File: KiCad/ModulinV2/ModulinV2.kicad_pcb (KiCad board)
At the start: 2 copper layers, 654 parts, among them IC1 TL074HIDR, IC10 ADS7866IDBVT, IC11 DAC60501ZDGSR, IC12 DAC60501ZDGSR, IC13 AS3340D, IC14 AS3340D, IC15 TL074HIDR, IC16 TL074HIDR, IC17 TL072HIDR, IC18 SN74LV10ADR, IC19 SN74LV10ADR, IC2 STM32F401RET6, IC20 SN74LV10ADR, IC21 SN74HC193DR, IC22 TMUX4051DYYRQ1, IC23 TL072HIDR, IC24 NC7SZ74K8X, IC25 SN74AHCT1G00DBVR, IC26 SN74AHCT1G00DBVR, IC27 SN74AHCT1G00DBVR, IC28 SN74AHC1G02DBVR, IC29 SN74AHC1G02DBVR, IC3 USBLC6-2SC6, IC30 SN74HC193DR, IC31 TMUX4052DYYR, IC32 TMUX4051DYYRQ1, IC33 TMUX4051DYYRQ1, IC34 E-ULN2003D1013TR, IC35 E-ULN2003D1013TR, IC36 CD4028BM96, IC37 CD4028BM96, IC38 TL072HIDR, IC39 AS3360D, IC4 TL072HIDR, IC40 REF196GSZ-REEL, IC41 NCP5500DADJR2G, IC42 LM2576S-12_NOPB, IC43 LM2576S-12_NOPB, IC44 REF195ESZ-REEL, IC45 NCP5500DADJR2G, IC46 L7812CD2T-TR, IC47 L7812CD2T-TR, IC48 TL074HIDR, IC49 AS3310D, IC5 TL072HIDR, IC50 AS3310D, IC51 TL074HIDR, IC52 DAC53202RTER, IC53 TL072HIDR, IC54 AS3320D, IC55 TL072HIDR, IC56 AS3320D, IC6 TL074HIDR, IC7 ADS7041IDCUR, IC8 ADS7041IDCUR, IC9 ADS7866IDBVT, J1 NRJ4HF-1, J2 USB4105-GF-A, J3 TSM-103-01-T-DV, J4 TSW-104-07-G-S, J5 TSW-104-07-T-D, J6 TSW-104-07-T-D, J7 TSW-104-07-T-D, J8 TSW-104-07-T-D, J9 PJ-002B, Q1 MMBFJ201, Q2 MMBFJ201, Q3 DMP610DL-7, SW1 SW_SPDT_MSM, SW2 Rocker Switch, U1 SN74AHC1G08DBVR, Y1 CX2016FB24000B0FZZH1

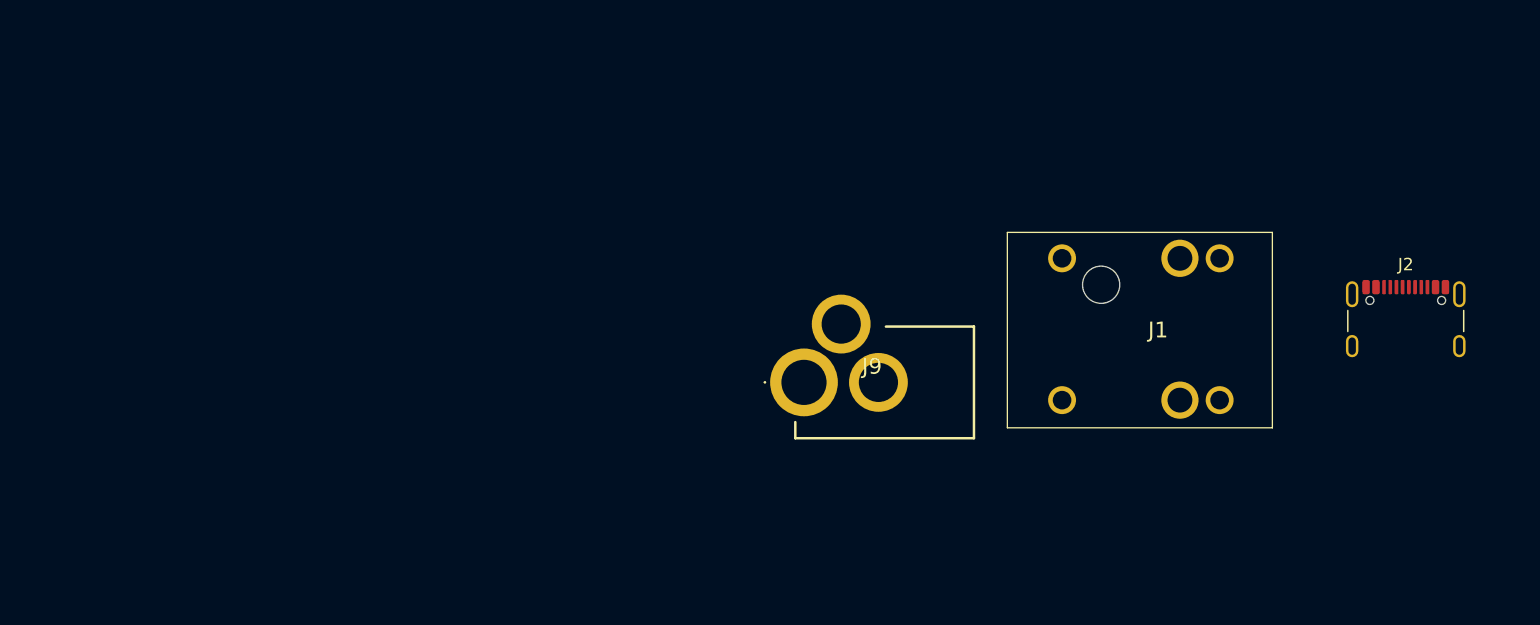
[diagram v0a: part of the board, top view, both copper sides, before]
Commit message: Finished Schematic, started on PCB
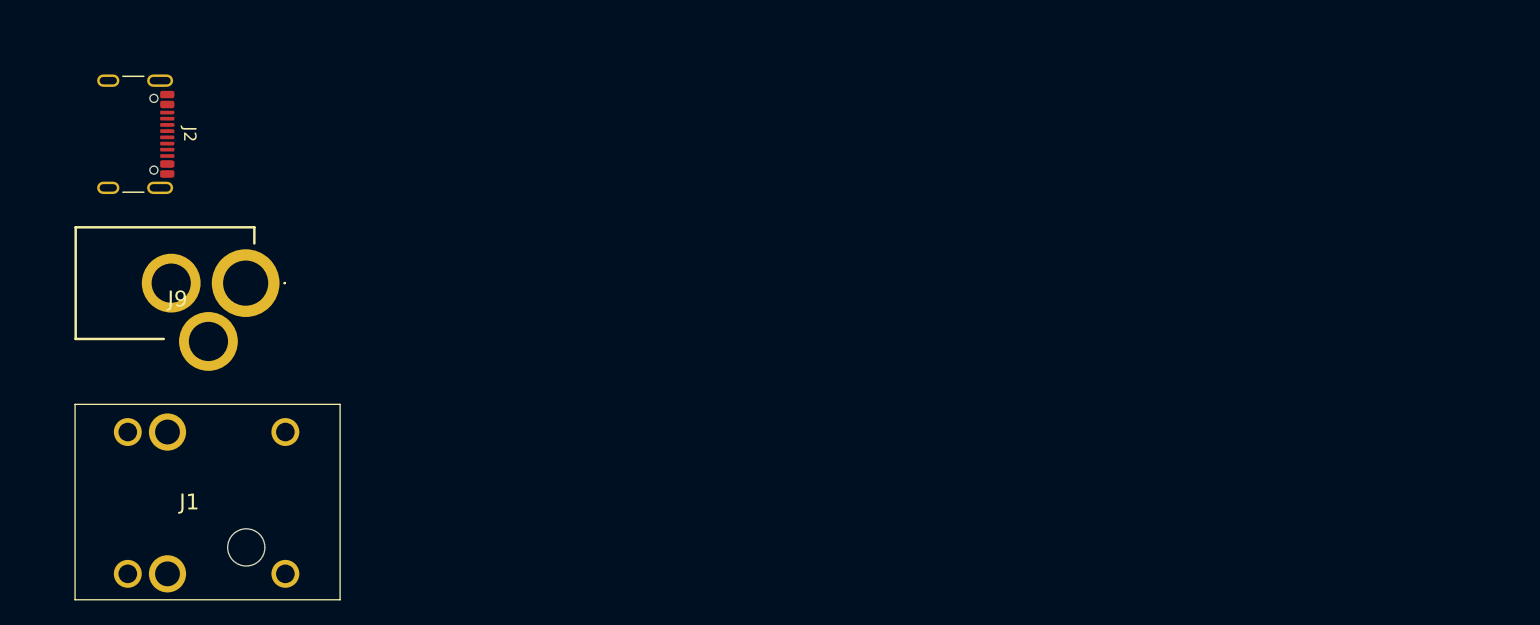
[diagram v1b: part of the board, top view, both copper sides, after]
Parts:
- moved J2 104.7 mm to (28.5, 169.0), turned to -90 degrees
- moved J1 62.7 mm to (41.7, 193.0), turned to 180 degrees
- moved J9 45.7 mm to (38.5, 181.0), turned to 180 degrees

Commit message: Started designing the power supply layout and grouped components by the type of circuit
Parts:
- C141, C142, IC46, IC47: moved to B.Cu
- moved C121 374.3 mm to (412.2, 121.9)
- moved C122 374.3 mm to (412.2, 124.4)
- moved C123 374.3 mm to (412.2, 126.9)
- moved C124 374.3 mm to (412.2, 129.4)
- moved C125 374.3 mm to (412.2, 131.9)
- moved C126 374.3 mm to (412.2, 134.4)
- moved C127 374.3 mm to (416.6, 121.9)
- moved C128 374.3 mm to (416.6, 124.4)
- moved C129 374.3 mm to (416.6, 126.9)
- moved C130 374.3 mm to (416.6, 129.4)
- moved C131 374.3 mm to (416.6, 131.9)
- moved IC38 374.3 mm to (414.3, 139.0)
- moved IC39 374.3 mm to (423.0, 125.9)
- moved R108 374.3 mm to (421.1, 132.5)
- moved R109 374.3 mm to (421.1, 135.4)
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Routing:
- net VDC: track 0.00 -> 116.0 mm
- net Net-(D7-A): track 0.00 -> 57.9 mm
- net -12V: track 0.00 -> 40.6 mm
- net Net-(IC42-FB): track 0.00 -> 37.4 mm
- net +12V: track 0.00 -> 29.6 mm
- net Net-(D6-K): track 0.00 -> 19.3 mm
- net Net-(D7-K): track 0.00 -> 18.9 mm
- net Net-(F1-Pad1): track 0.00 -> 8.55 mm
- net GND: track 0.00 -> 8.11 mm
- net Net-(Q3-D): track 0.00 -> 6.55 mm
- added copper zone on B.Cu, net GND
- added copper zone on F.Cu, net GND
- added copper zone on In1.Cu, net GND
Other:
- copper layers 2 -> 4

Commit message: Layed out Interface and PWR components and started with MCU layout
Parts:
- removed the C39 at (376.1, 79.7)
- removed the C40 at (376.1, 82.2)
- C10, C11, C12, C13, C14, C15, C16, C17, C18, C19, C22, C24, C27, C30, C33, C35, C37, C7, C8, C9, D7, IC41, IC43, IC5, IC6, L2, L4, R112, R21, R22, R23, R24, R25, R29, R30, R31, R32, R33, RV2, RV3: moved to B.Cu
- C139: renamed from C141; moved to F.Cu
- IC46: moved to F.Cu
- moved J3 357.5 mm to (21.5, 108.5), turned to 90 degrees
- moved C6 335.0 mm to (29.5, 86.5), turned to 180 degrees
- moved TP3 331.2 mm to (30.0, 95.5)
- moved C13 319.9 mm to (51.1, 89.8)
- moved C11 319.6 mm to (51.1, 83.8)
- moved C12 318.4 mm to (51.1, 80.8)
- moved C16 318.1 mm to (51.1, 86.8)
- moved C18 317.6 mm to (48.1, 92.8), turned to 180 degrees
- moved C17 316.9 mm to (53.1, 92.8)
- moved C9 313.4 mm to (58.1, 83.8), turned to -90 degrees
- moved C14 312.4 mm to (59.1, 93.8), turned to 90 degrees
- moved C7 310.4 mm to (57.6, 90.3)
- moved D1 310.0 mm to (26.5, 87.4), turned to -90 degrees
- moved C15 309.3 mm to (55.1, 82.8), turned to -90 degrees
- moved C10 308.7 mm to (57.6, 87.0)
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- renumbered C102 to C100, C103 to C101, C104 to C102, C105 to C103, C106 to C104, C107 to C105, C108 to C106, C109 to C107, C110 to C108, C111 to C109, C112 to C110, C113 to C111, C114 to C112, C115 to C113, C116 to C114, C117 to C115, C118 to C116, C119 to C117, C120 to C118, C121 to C119, C122 to C120, C123 to C121, C124 to C122, C125 to C123, C126 to C124, C127 to C125, C128 to C126, C129 to C127, C130 to C128, C131 to C129, C132 to C130, C133 to C131, C134 to C132, C135 to C133, C136 to C134, C137 to C135, C138 to C136, C139 to C137, C140 to C138, C142 to C140, C143 to C141, C144 to C142, C145 to C143, C146 to C144, C147 to C145, C148 to C146, C149 to C147, C150 to C148, C151 to C149, C152 to C150, C153 to C151, C154 to C152, C155 to C153, C156 to C154, C157 to C155, C158 to C156, C159 to C157, C160 to C158, C161 to C159, C162 to C160, C163 to C161, C164 to C162, C165 to C163, C166 to C164, C167 to C165, C168 to C166, C169 to C167, C170 to C168, C171 to C169, C172 to C170, C173 to C171, C174 to C172, C175 to C173, C176 to C174, C177 to C175, C178 to C176, C179 to C177, C180 to C178, C181 to C179, C182 to C180, C183 to C181, C184 to C182, C185 to C183, C186 to C184, C187 to C185, C188 to C186, C189 to C187, C190 to C188, C191 to C189, C192 to C190, C193 to C191, C194 to C192, C195 to C193, C196 to C194, C197 to C195, C198 to C196, C199 to C197, C200 to C198, C201 to C199, C202 to C200, C203 to C201, C204 to C202, C205 to C203, C206 to C204, C207 to C205, C208 to C206, C209 to C207, C210 to C208, C211 to C209, C212 to C210, C213 to C211, C214 to C212, C215 to C213, C216 to C214, C217 to C215, C41 to C39, C43 to C40, C42 to C41, C44 to C42, C45 to C43, C46 to C44, C47 to C45, C48 to C46, C49 to C47, C50 to C48, C51 to C49, C52 to C50, C53 to C51, C54 to C52, C55 to C53, C56 to C54, C57 to C55, C58 to C56, C59 to C57, C60 to C58, C61 to C59, C62 to C60, C63 to C61, C64 to C62, C65 to C63, C66 to C64, C67 to C65, C68 to C66, C69 to C67, C70 to C68, C71 to C69, C72 to C70, C73 to C71, C74 to C72, C75 to C73, C76 to C74, C77 to C75, C78 to C76, C79 to C77, C80 to C78, C81 to C79, C82 to C80, C83 to C81, C84 to C82, C85 to C83, C86 to C84, C87 to C85, C88 to C86, C89 to C87, C90 to C88, C91 to C89, C92 to C90, C93 to C91, C94 to C92, C95 to C93, C96 to C94, C97 to C95, C98 to C96, C99 to C97, C100 to C98, C101 to C99, TP96 to TP92, TP92 to TP93, TP93 to TP94, TP94 to TP95, TP97 to TP96, TP95 to TP97
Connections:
- IC2 pad 19: unconnected-(IC2-VDD_1-Pad19) -> +3.3V
- IC2 pad 44: /MCU/USB_DM -> /MCU/USB_D-
- IC2 pad 45: /MCU/USB_DP -> /MCU/USB_D+
- IC2 pad 64: unconnected-(IC2-VDD_4-Pad64) -> +3.3V
- IC3 pad 4: /MCU/USB_DP -> /MCU/USB_D+
- IC3 pad 6: /MCU/USB_DM -> /MCU/USB_D-
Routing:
- net +12V: track 29.6 -> 114.8 mm, vias 0 -> 1
- net +3.3V: track 0.00 -> 70.0 mm, vias 0 -> 5
- net -12V: track 40.6 -> 92.4 mm, vias 0 -> 2
- net +3.3VA: track 0.00 -> 46.7 mm, vias 0 -> 4
- net Net-(IC5A--): track 0.00 -> 41.8 mm
- net /ADSR/GATE2: track 0.00 -> 41.8 mm
- net Net-(IC5B--): track 0.00 -> 41.7 mm
- net +5V: track 0.00 -> 35.7 mm, vias 0 -> 1
- net /PRESSURE1: track 0.00 -> 35.6 mm
- net /PRESSURE2: track 0.00 -> 31.9 mm, vias 0 -> 2
- net /ADSR/GATE1: track 0.00 -> 30.8 mm
- net /Interface/AINP2: track 0.00 -> 30.1 mm
- net /MCU/VBUS: track 0.00 -> 28.8 mm
- net VDC: track 116.0 -> 144.6 mm
- net /Interface/AINP1: track 0.00 -> 28.0 mm
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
